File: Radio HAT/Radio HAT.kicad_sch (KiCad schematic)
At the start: 43 parts, among them J1 Raspberry_Pi_2_3, J2 Coax SMA, J3 Barrel_Jack, J4 VCC, J5 6V, J6 GND, J7 V_RF, J8 GPIO, Q1 NMOS, U1 RFM98PW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

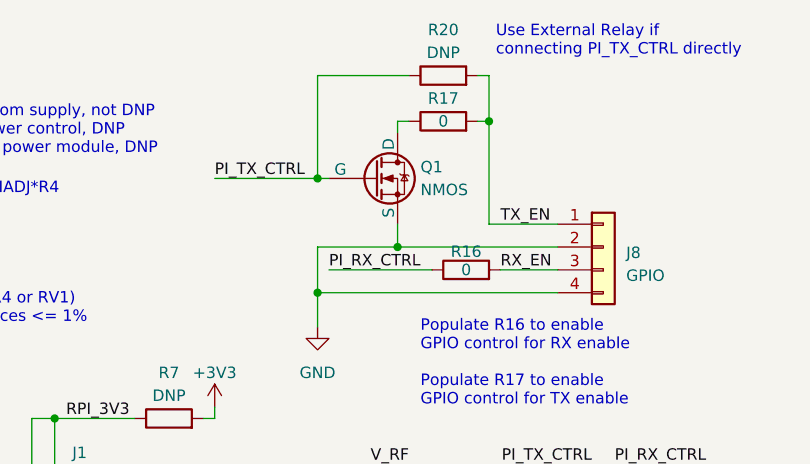
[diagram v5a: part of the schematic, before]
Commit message: Fixed Q1 footprint
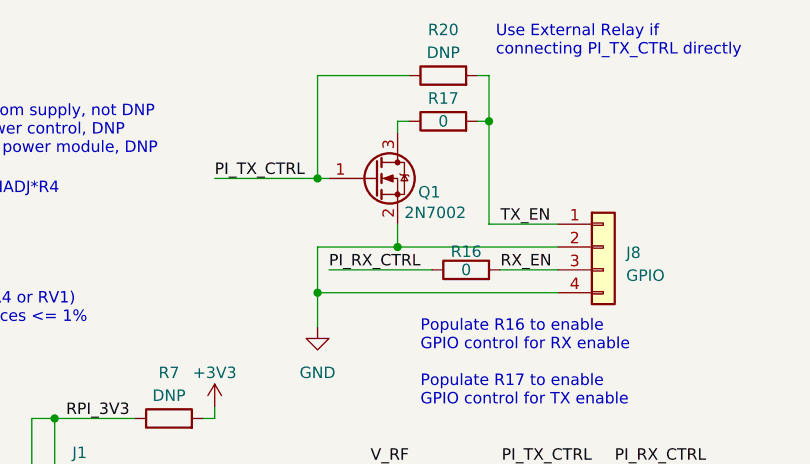
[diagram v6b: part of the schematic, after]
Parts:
- removed Q1: NMOS, Package_TO_SOT_SMD:SOT-23-3, symbol Simulation_SPICE:NMOS
- added Q1: 2N7002, Package_TO_SOT_SMD:SOT-23, symbol Transistor_FET:2N7002
- U2: value AZ2185D-ADJTRG1 -> AZ2185D-ADJTRG1
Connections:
- net GND: now also Q1.2 (S)
- net PI_TX_CTRL: now also Q1.1 (G)
- net at R17.1: now also Q1.3 (D)
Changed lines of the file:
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@@
+	)
+	(symbol
+		(lib_id "Transistor_FET:2N7002")
+		(at 224.79 40.64 0)
+		(unit 1)
+		(exclude_from_sim no)
+		(in_bom yes)
+		(on_board yes)
+		(dnp no)
+		(property "Reference" "Q1"
+			(at 229.616 42.164 0)
+			(effects
+				(font
+					(size 1.27 1.27)
+				)
+				(justify left)
+			)
+		)
+		(property "Value" "2N7002"
+			(at 228.092 44.45 0)
+			(effects
+				(font
+					(size 1.27 1.27)
+				)
+				(justify left)
+			)
+		)
+		(property "Footprint" "Package_TO_SOT_SMD:SOT-23"
+			(at 229.87 42.545 0)
+			(effects
+				(font
+					(size 1.27 1.27)
+					(italic yes)
+				)
+				(justify left)
+				(hide yes)
+			)
+		)
+		(property "Datasheet" "https://www.onsemi.com/pub/Collateral/NDS7002A-D.PDF"
+			(at 229.87 44.45 0)
+			(effects
+				(font
+					(size 1.27 1.27)
+				)
+				(justify left)
+				(hide yes)
+			)
+		)
+		(property "Description" "0.115A Id, 60V Vds, N-Channel MOSFET, SOT-23"
+			(at 224.79 40.64 0)
+			(effects
+				(font
+					(size 1.27 1.27)
+				)
+				(hide yes)
+			)
+		)
+		(pin "2"
+		)
+		(pin "1"
+		)
+		(pin "3"
+		)
+		(instances
+			(project ""
+				(path "/e833ba5c-90ae-4111-9eec-1a872963763a"
+					(reference "Q1")
+					(unit 1)
+				)
+			)
+		)
 	)
 	(symbol
@@
 			)
 		)
-		(property "Value" "AZ2185D-ADJTRG1\n"
+		(property "Value" "AZ2185D-ADJTRG1"
 			(at 93.98 39.37 0)
 			(effects
@@
 					(unit 1)
 				)
-			)
-		)
-	)
-	(symbol
-		(lib_id "Simulation_SPICE:NMOS")
-		(at 224.79 40.64 0)
-		(unit 1)
-		(exclude_from_sim no)
-		(in_bom yes)
-		(on_board yes)
-		(dnp no)
-		(property "Reference" "Q1"
-			(at 229.87 39.37 0)
-			(effects
-				(font
-					(size 1.27 1.27)
-				)
-				(justify left)
-			)
-		)
-		(property "Value" "NMOS"
-			(at 229.87 41.91 0)
-			(effects
-				(font
-					(size 1.27 1.27)
-				)
-				(justify left)
-			)
-		)
-		(property "Footprint" "Package_TO_SOT_SMD:SOT-23-3"
-			(at 229.87 38.1 0)
-			(effects
-				(font
-					(size 1.27 1.27)
-				)
-				(hide yes)
-			)
-		)
-		(property "Datasheet" "https://ngspice.sourceforge.io/docs/ngspice-manual.pdf"
-			(at 224.79 53.34 0)
-			(effects
-				(font
-					(size 1.27 1.27)
-				)
-				(hide yes)
-			)
-		)
-		(property "Description" ""
-			(at 224.79 40.64 0)
-			(effects
-				(font
-					(size 1.27 1.27)
-				)
-				(hide yes)
-			)
-		)
-		(property "Sim.Device" "NMOS"
-			(at 224.79 57.785 0)
-			(effects
-				(font
-					(size 1.27 1.27)
-				)
-				(hide yes)
-			)
-		)
-		(property "Sim.Type" "VDMOS"
-			(at 224.79 59.69 0)
-			(effects
-				(font
-					(size 1.27 1.27)
-				)
-				(hide yes)
-			)
-		)
-		(property "Sim.Pins" "1=D 2=G 3=S"
-			(at 224.79 55.88 0)
-			(effects
-				(font
-					(size 1.27 1.27)
-				)
-				(hide yes)
-			)
-		)
-		(pin "1"
-		)
-		(pin "2"
-		)
-		(pin "3"
-		)
-		(instances
-			(project "Radio HAT"
-				(path "/e833ba5c-90ae-4111-9eec-1a872963763a"
-					(reference "Q1")
-					(unit 1)
-				)
